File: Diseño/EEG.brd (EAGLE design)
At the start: 49.8 x 80 mm, 42 parts, among them IC1 REF2033AIDDCT, IC2 MCP73831T-2ACI_OT, IC3 LP38692MP-3.3_NOPB, J1 USB3500-30-A-KIT, J2 SJ3-35083A-TR, J3 1769

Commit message: correciones de conexion
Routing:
- net N$16: track 25.5 -> 22.9 mm
- net +3V3: track 130.1 -> 132.1 mm, vias 6 -> 9
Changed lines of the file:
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@@
 <contactref element="LP1" pad="5"/>
 <contactref element="IC3" pad="3"/>
-<wire x1="10.615" y1="55.7" x2="7.935" y2="53.02" width="0.1524" layer="1"/>
 <wire x1="19.685" y1="51.12" x2="24.13" y2="51.12" width="0.1524" layer="1"/>
 <wire x1="7.62" y1="29.038" x2="6.985" y2="29.673" width="0.1524" layer="1"/>
@@
 <via x="24.13" y="48.26" extent="1-16" drill="0.35"/>
 <wire x1="24.13" y1="48.26" x2="24.13" y2="51.12" width="0.1524" layer="1"/>
-<wire x1="10.615" y1="57.29" x2="10.615" y2="55.7" width="0.1524" layer="1"/>
-<via x="3.81" y="49.53" extent="1-16" drill="0.35"/>
-<wire x1="3.81" y1="49.53" x2="8.89" y2="54.61" width="0.1524" layer="16"/>
-<wire x1="14.605" y1="54.61" x2="8.89" y2="54.61" width="0.1524" layer="16"/>
-<wire x1="14.605" y1="54.61" x2="19.685" y2="49.53" width="0.1524" layer="16"/>
 <via x="19.685" y="49.53" extent="1-16" drill="0.35"/>
-<wire x1="1.905" y1="53.02" x2="3.175" y2="53.02" width="0.1524" layer="1"/>
-<wire x1="3.175" y1="53.02" x2="3.81" y2="52.385" width="0.1524" layer="1"/>
-<wire x1="3.81" y1="52.385" x2="3.81" y2="49.53" width="0.1524" layer="1"/>
 <wire x1="19.685" y1="51.12" x2="19.685" y2="49.53" width="0.1524" layer="1"/>
-<wire x1="14.605" y1="54.61" x2="7.935" y2="53.02" width="0" layer="19" extent="1-1"/>
+<wire x1="1.905" y1="53.02" x2="5.395" y2="53.02" width="0.1524" layer="1"/>
+<wire x1="5.395" y1="53.02" x2="7.62" y2="55.245" width="0.1524" layer="1"/>
+<wire x1="10.615" y1="57.29" x2="10.795" y2="57.11" width="0.1524" layer="1"/>
+<wire x1="10.795" y1="57.11" x2="10.795" y2="55.88" width="0.1524" layer="1"/>
+<wire x1="10.795" y1="55.88" x2="10.16" y2="55.245" width="0.1524" layer="1"/>
+<wire x1="10.16" y1="55.245" x2="7.62" y2="55.245" width="0.1524" layer="1"/>
+<via x="19.685" y="49.53" extent="1-16" drill="0.35"/>
+<wire x1="19.685" y1="49.53" x2="17.78" y2="47.625" width="0.1524" layer="16"/>
+<wire x1="17.78" y1="47.625" x2="17.145" y2="47.625" width="0.1524" layer="16"/>
+<wire x1="17.145" y1="47.625" x2="17.145" y2="47.9006" width="0.1524" layer="16"/>
+<via x="17.145" y="47.9006" extent="1-16" drill="0.35"/>
+<wire x1="17.145" y1="47.9006" x2="16.1506" y2="48.895" width="0.1524" layer="1"/>
+<via x="13.97" y="48.895" extent="1-16" drill="0.35"/>
+<wire x1="13.333425" y1="49.531575" x2="5.713425" y2="49.531575" width="0.1524" layer="16"/>
+<via x="5.713425" y="49.531575" extent="1-16" drill="0.35"/>
+<wire x1="5.713425" y1="49.531575" x2="2.225" y2="53.02" width="0.1524" layer="1"/>
+<wire x1="2.225" y1="53.02" x2="1.905" y2="53.02" width="0.1524" layer="1"/>
+<wire x1="16.1506" y1="48.895" x2="13.97" y2="48.895" width="0.1524" layer="1"/>
+<wire x1="13.97" y1="48.895" x2="13.333425" y2="49.531575" width="0.1524" layer="16"/>
 </signal>
 <signal name="GND">
@@
 <wire x1="15.695" y1="55.425" x2="17.145" y2="53.975" width="0.1524" layer="1"/>
 <via x="17.145" y="53.975" extent="1-16" drill="0.35"/>
-<wire x1="17.145" y1="53.975" x2="17.145" y2="51.435" width="0.1524" layer="16"/>
 <via x="17.145" y="51.435" extent="1-16" drill="0.35"/>
 <wire x1="17.145" y1="51.435" x2="17.145" y2="48.895" width="0.1524" layer="1"/>
@@
 <wire x1="10.16" y1="46.355" x2="8.67" y2="46.355" width="0.1524" layer="1"/>
 <wire x1="8.67" y1="46.355" x2="8.255" y2="46.77" width="0.1524" layer="1"/>
+<wire x1="17.145" y1="51.435" x2="17.145" y2="53.975" width="0" layer="19" extent="1-1"/>
 </signal>
 <signal name="N$17">
@@
 <wire x1="15.24" y1="53.02" x2="19.685" y2="53.02" width="0.1524" layer="1"/>
 <wire x1="19.685" y1="53.02" x2="18.415" y2="51.75" width="0.1524" layer="1"/>
+<wire x1="18.415" y1="49.53" x2="21.595" y2="46.35" width="0.1524" layer="1"/>
+<wire x1="27.965" y1="46.35" x2="21.595" y2="46.35" width="0.1524" layer="1"/>
 <wire x1="18.415" y1="51.75" x2="18.415" y2="49.53" width="0.1524" layer="1"/>
-<wire x1="21.595" y1="46.35" x2="18.415" y2="49.53" width="0.1524" layer="1"/>
-<wire x1="27.965" y1="46.35" x2="21.595" y2="46.35" width="0.1524" layer="1"/>
 </signal>
 <signal name="N$15">

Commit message: arreglé todas las vias de la PCB
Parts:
- moved INA_1 0.63 mm to (5.71, 32.4)
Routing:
- net +3V3: track 132.1 -> 164.6 mm, vias 9 -> 10
- net CS1: track 21.0 -> 0.00 mm
- net N$19: track 25.5 -> 44.9 mm, vias 0 -> 2
- net CS2: track 17.3 -> 0.88 mm
- net N$18: track 19.3 -> 31.5 mm, vias 4 -> 0
- net O4: track 23.0 -> 32.0 mm, vias 4 -> 2
- net USB_3: track 64.0 -> 55.2 mm
- net VSS: track 111.7 -> 104.1 mm
- net N$13: track 51.6 -> 58.8 mm, vias 0 -> 2
- net N$11: track 20.7 -> 27.8 mm
- net +BATT: track 17.7 -> 10.9 mm
- net N$16: track 22.9 -> 16.4 mm, vias 6 -> 2
- net N$2: track 29.8 -> 34.6 mm, vias 2 -> 0
- net N$15: track 23.3 -> 27.6 mm
- net N$17: track 20.0 -> 23.7 mm, vias 2 -> 0
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
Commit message: Se agregaron los planos de tierra y se corregieron algunas pistas
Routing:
- net CS1: track 0.00 -> 27.8 mm, vias 0 -> 2
- net CS2: track 0.88 -> 15.6 mm, vias 0 -> 1
- net VSS: track 104.1 -> 118.9 mm
- net N$7: track 18.3 -> 26.4 mm
- net USB_3: track 55.2 -> 60.8 mm
- net N$6: track 13.5 -> 16.9 mm, vias 0 -> 2
- net +3V3: track 164.6 -> 167.7 mm, vias 10 -> 9
- net O1: track 48.2 -> 51.2 mm
- net N$19: track 44.9 -> 47.4 mm
- net N$11: track 27.8 -> 29.1 mm
- net O3: track 46.6 -> 47.2 mm
- net N$17: track 23.7 -> 23.8 mm, vias 0 -> 2
- added copper zone on layer 1, net GND
- added copper zone on layer 16, net GND

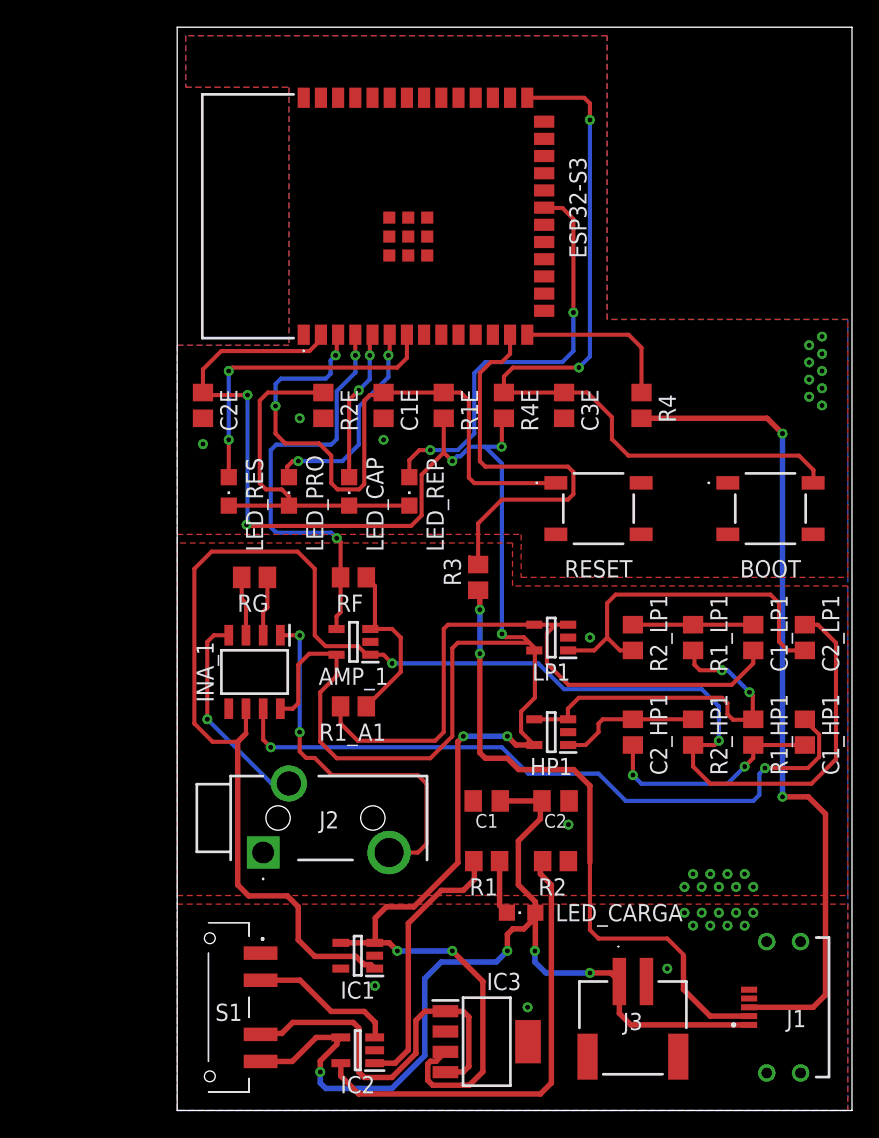
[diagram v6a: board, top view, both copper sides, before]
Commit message: Se agregaron los touchpads
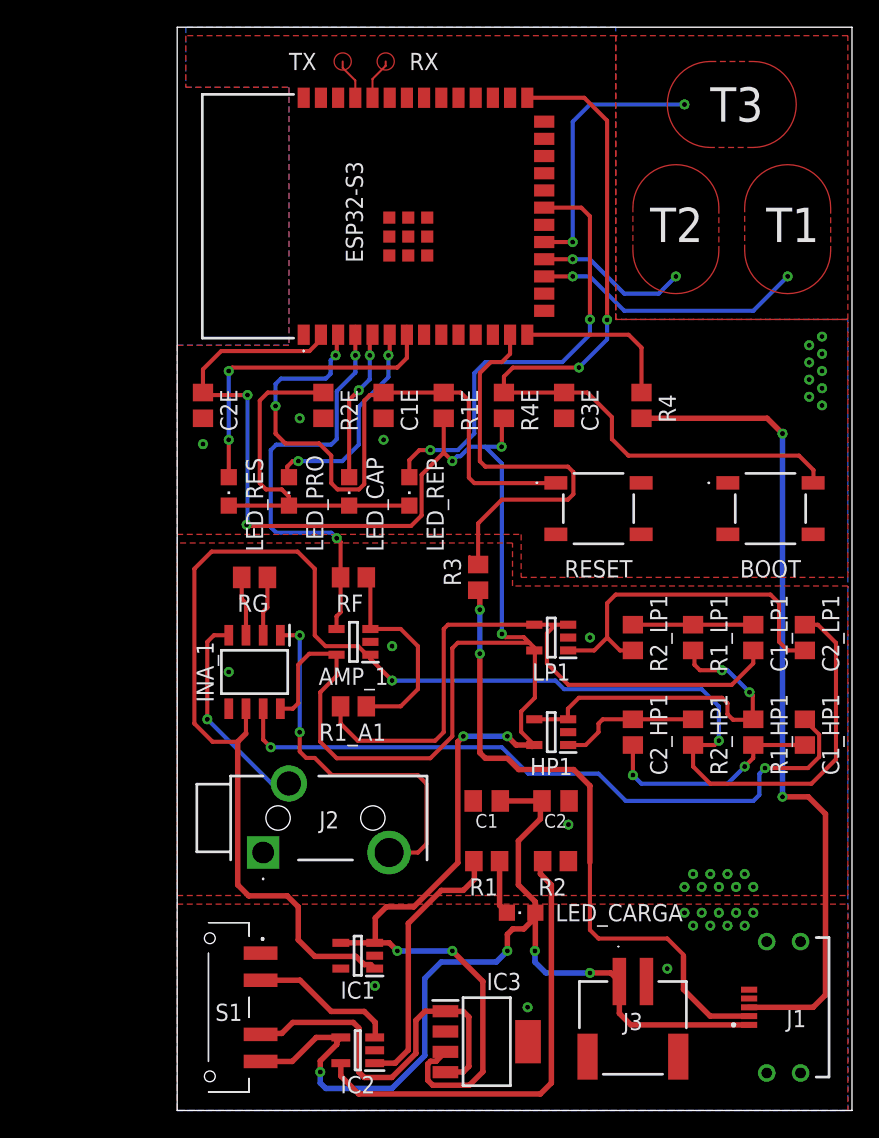
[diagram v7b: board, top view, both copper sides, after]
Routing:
- net TOUCHP_1: track 0.00 -> 20.1 mm, vias 0 -> 2
- net TOUCHP_3: track 0.00 -> 19.8 mm, vias 0 -> 2
- net TOUCHP_2: track 0.00 -> 11.3 mm, vias 0 -> 2
- net RX: track 0.00 -> 3.08 mm
- net TX: track 0.00 -> 3.07 mm
- net N$8: track 12.7 -> 15.5 mm
- net LED_REP: track 31.6 -> 33.5 mm
- net N$13: track 58.8 -> 59.9 mm
- added copper zone on layer 1, net RX
- added copper zone on layer 1, net TOUCHP_1
- added copper zone on layer 1, net TOUCHP_2
- added copper zone on layer 1, net TOUCHP_3
- added copper zone on layer 1, net TX
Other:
- board text added: "RX"
- board text added: "T1"
- board text added: "T2"
- board text added: "T3"
- board text added: "TX"
